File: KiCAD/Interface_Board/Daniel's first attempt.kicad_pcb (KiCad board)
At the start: 2 copper layers, 200.7 x 92.2 mm, 36 parts, among them J1 TB001-500-04BE, J2 Conn_02x15_Top_Bottom

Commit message: Reminder: Need to change diameter of TP points from 2.0mm to 1.75mm before sign off
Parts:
- removed H10: TP 15, TestPoint:TestPoint_Plated_Hole_D2.0mm
- removed H11: TP 16, TestPoint:TestPoint_Plated_Hole_D2.0mm
- moved TP16-AuxIN1 7.73 mm to (140.2, 60.3)
- moved TP17-GuitarIn1 7.18 mm to (189.7, 63.8)
- renumbered H3 to +12V1, TP25 to CCW-D1, TP24 to CCW-T1, TP28 to CCW-V1, TP18 to CW-D1, TP19 to CW-T1, TP27 to CW-V1, TP26 to PresenceIN1, TP22 to PresenceOut1, TP1 to TP1-GND1, TP10 to TP10-EmitterFollowerOut1, TP11 to TP11-PosDriverOut1, TP13 to TP13-SourceFollowerOut1, H2 to TP14-SPKR-1, TP29 to TP16-AuxIN1, TP17 to TP17-GuitarIn1, TP2 to TP2-GND1, TP3 to TP3-12V1, TP4 to TP4-PreampOut1, TP5 to TP5-8Vout1, TP6 to TP6-GainStageOut1, TP7 to TP7-EmitterBypassOut1, TP8 to TP8-6Vout1, TP9 to TP9-NegDriverOut1, H1 to Tp12-SPKR+1, TP20 to W-D1, TP21 to W-T1, TP23 to W-V1
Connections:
- J2 pad 13: noconnection -> Net-(J2-Pad13)
- J2 pad 14: noconnection -> Net-(J2-Pad14)
- J2 pad 15: noconnection -> Net-(J2-Pad15)
- J2 pad 27: noconnection -> Net-(J2-Pad27)
- J2 pad 28: noconnection -> Net-(J2-Pad28)
- J2 pad 29: noconnection -> Net-(J2-Pad29)
- J2 pad 30: noconnection -> Net-(J2-Pad30)
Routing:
- net AUXR: track 108.1 -> 118.2 mm
- net DRIVEW: track 152.2 -> 146.4 mm
- net DRIVECW: track 111.4 -> 107.5 mm
- net GuitarIn: track 92.9 -> 89.0 mm
- net GND: vias 14 -> 13
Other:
- board text added: "Change Diameter of drill size before Manufactured (1.75mm)"
- board text removed: "Pogo Board YOOO"

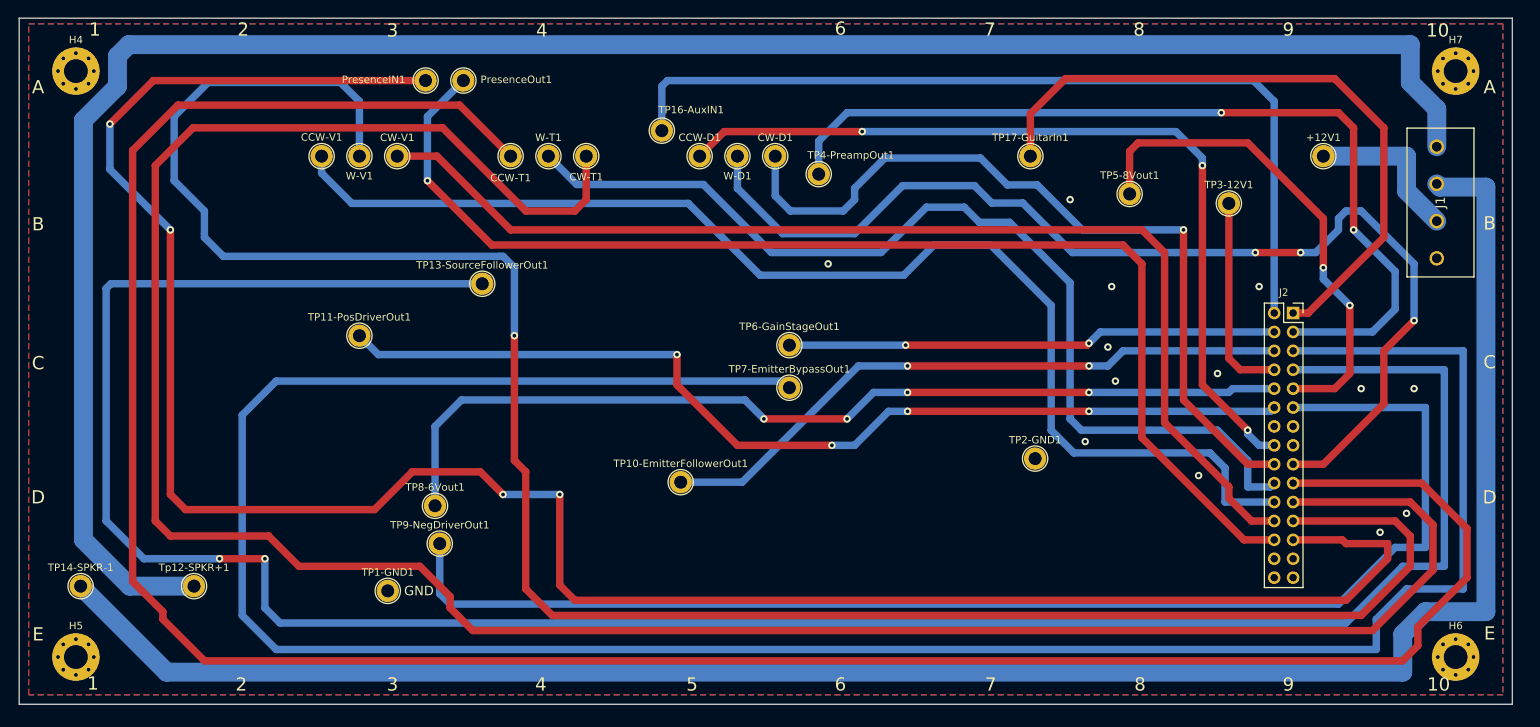
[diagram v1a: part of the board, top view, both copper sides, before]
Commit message: Zero Vias needed :)!! added vias only for GND if necessary. Note: Since we are plugging in the cable to the bottom of the testboard, the ribbon cable will be flipped therefore, the test points on the ribbon will be flipped. I swapped the couples for each row accordingly. So far if we get the green light from Mark, This baby will be read to show tomorrow to Professor Dorr.
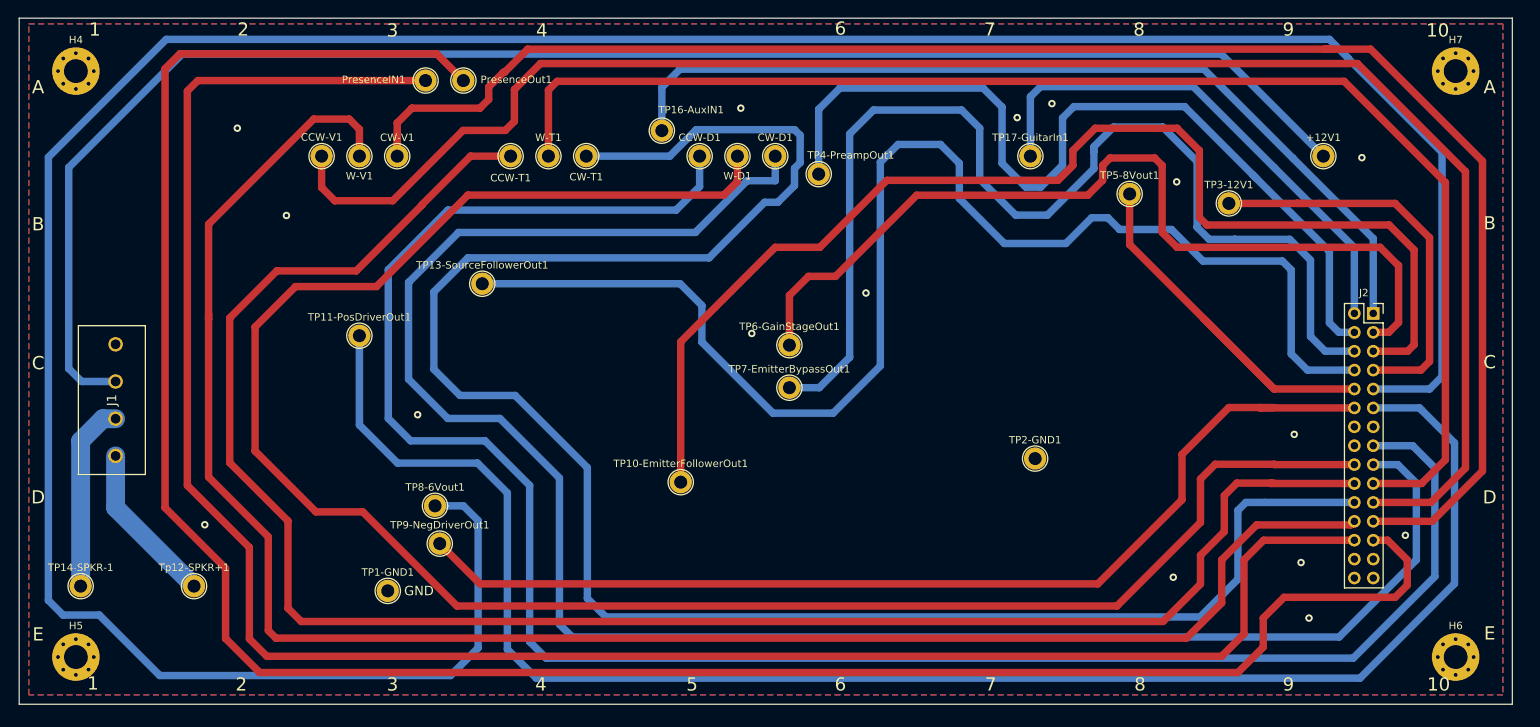
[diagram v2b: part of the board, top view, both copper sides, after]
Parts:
- moved J1 182.3 mm to (66.8, 104.0), turned to 90 degrees
- moved J2 10.8 mm to (235.8, 84.9)
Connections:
- J2 pad 1: GuitarIn -> AUXR
- J2 pad 10: 6VOut -> 8VOut
- J2 pad 11: NEGDriverOut -> POSDriverOut
- J2 pad 12: POSDriverOut -> NEGDriverOut
- J2 pad 15: Net-(J2-Pad15) -> DRIVECCW
- J2 pad 16: DRIVECCW -> Net-(J2-Pad16)
- J2 pad 17: DRIVEW -> DRIVECW
- J2 pad 18: DRIVECW -> DRIVEW
- J2 pad 19: TONECCW -> TONEW
- J2 pad 2: AUXR -> GuitarIn
- J2 pad 20: TONEW -> TONECCW
- J2 pad 21: TONECW -> VOLUMECCW
- J2 pad 22: VOLUMECCW -> TONECW
- J2 pad 23: VolumeW -> VolumeCW
- J2 pad 24: VolumeCW -> VolumeW
- J2 pad 25: PresenceIn -> PresenceOUT
- J2 pad 26: PresenceOUT -> PresenceIn
- J2 pad 3: PreampOut -> GainStageOut
- J2 pad 4: GainStageOut -> PreampOut
- J2 pad 5: EmitterBypassOut -> EmitterFollowerOut
- J2 pad 6: EmitterFollowerOut -> EmitterBypassOut
- J2 pad 7: SourceFollowerOut -> 12VDC
- J2 pad 8: 12VDC -> SourceFollowerOut
- J2 pad 9: 8VOut -> 6VOut
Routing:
- net 6VOut: track 127.7 -> 387.0 mm, vias 4 -> 0
- net Speaker+: track 273.9 -> 21.9 mm
- net Speaker-: track 263.8 -> 25.4 mm
- net +12V: track 21.6 -> 214.6 mm
- net EmitterBypassOut: track 329.3 -> 149.2 mm
- net DRIVECCW: track 114.2 -> 265.5 mm, vias 3 -> 0
- net DRIVECW: track 107.5 -> 254.0 mm, vias 1 -> 0
- net SourceFollowerOut: track 321.3 -> 183.1 mm, vias 2 -> 0
- net PresenceOUT: track 162.9 -> 299.3 mm, vias 1 -> 0
- net DRIVEW: track 146.4 -> 260.7 mm, vias 3 -> 0
- net TONECCW: track 337.0 -> 246.3 mm
- net POSDriverOut: track 133.5 -> 222.6 mm, vias 4 -> 0
- net EmitterFollowerOut: track 87.1 -> 161.1 mm, vias 2 -> 0
- net VolumeCW: track 152.4 -> 221.8 mm
- net TONECW: track 327.1 -> 262.0 mm
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
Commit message: Final Rev 1. Sent To mark to mil, hopefully have before End of Day
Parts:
- added GNDP1: GND, TestPoint:TestPoint_Plated_Hole_D2.0mm, F.Cu at (222.8, 75.2)
- H4, H5, H6, H7: footprint MountingHole:MountingHole_3.2mm_M3_Pad_Via -> MountingHole:MountingHole_3.7mm_Pad_Via
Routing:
- net SourceFollowerOut: track 183.1 -> 176.5 mm
- net EmitterBypassOut: track 149.2 -> 142.8 mm
- net GainStageOut: track 120.2 -> 117.9 mm
- net EmitterFollowerOut: track 161.1 -> 159.5 mm
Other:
- board text removed: "Change Diameter of drill size before Manufactured (1.75mm)"

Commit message: Missed one
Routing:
- net PreampOut: track 118.7 -> 140.3 mm, vias 0 -> 1
- net 8VOut: track 58.3 -> 49.4 mm, vias 0 -> 1
- net EmitterBypassOut: track 142.8 -> 150.1 mm, vias 0 -> 1
- net NEGDriverOut: track 140.5 -> 133.7 mm, vias 0 -> 1
- net DRIVEW: track 260.7 -> 254.8 mm, vias 0 -> 1
- net 6VOut: track 387.0 -> 392.7 mm, vias 0 -> 1
- net TONECCW: track 246.3 -> 241.3 mm, vias 0 -> 1
- net DRIVECW: track 254.0 -> 258.9 mm, vias 0 -> 1
- net VolumeCW: track 221.8 -> 225.0 mm, vias 0 -> 3
- net SourceFollowerOut: track 176.5 -> 173.6 mm, vias 0 -> 1
- net VOLUMECCW: track 229.0 -> 230.9 mm, vias 0 -> 3
- net PresenceOUT: track 299.3 -> 297.4 mm, vias 0 -> 1
- net VolumeW: track 245.3 -> 243.8 mm, vias 0 -> 1
- net 12VDC: track 54.6 -> 55.9 mm, vias 0 -> 3
- net Speaker-: track 25.4 -> 26.5 mm, vias 0 -> 1
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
